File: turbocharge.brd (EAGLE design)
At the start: 56.2 x 21 mm, 87 parts, among them Q1 NMOS40V_10A, Q11 NMOS40V_10A, Q12 NMOS40V_10A, Q14 NMOS40V_10A, Q16 2PMOS50V_0.17A, Q18 NMOS40V_10A, Q2 NMOS40V_10A, Q21 PMOS30V_11A, Q22 PMOS30V_11A, Q23 NMOS40V_10A, Q24 NMOS40V_10A, Q25 PMOS30V_11A, Q26 PMOS30V_11A, Q27 NMOS40V_10A, Q28 NMOS40V_10A, Q31 PMOS30V_11A, Q32 PMOS30V_11A, Q33 PMOS30V_11A, Q34 PMOS30V_11A, Q35 PMOS30V_11A, Q36 PMOS30V_11A, Q37 PMOS30V_11A, Q38 PMOS30V_11A, Q41 PMOS30V_11A, Q42 PMOS30V_11A, Q43 PMOS30V_11A, Q44 PMOS30V_11A, Q45 PMOS30V_11A, Q46 PMOS30V_11A, Q47 PMOS30V_11A, Q48 PMOS30V_11A, Q51 PMOS30V_11A, Q52 PMOS30V_11A, Q53 PMOS30V_11A, Q54 PMOS30V_11A, Q55 PMOS30V_11A, Q56 PMOS30V_11A, Q57 PMOS30V_11A, Q58 PMOS30V_11A, Q62 PMOS30V_11A, Q64 PMOS30V_11A, Q66 PMOS30V_11A, Q68 PMOS30V_11A, T1 TFORM_4_4311_4A4, U1 LT3757IDD, U10 CCR20MA_45V, U2 TC1240A, U4 2NMOS30V_0.1A, U5 74HC595, U6 74HC595

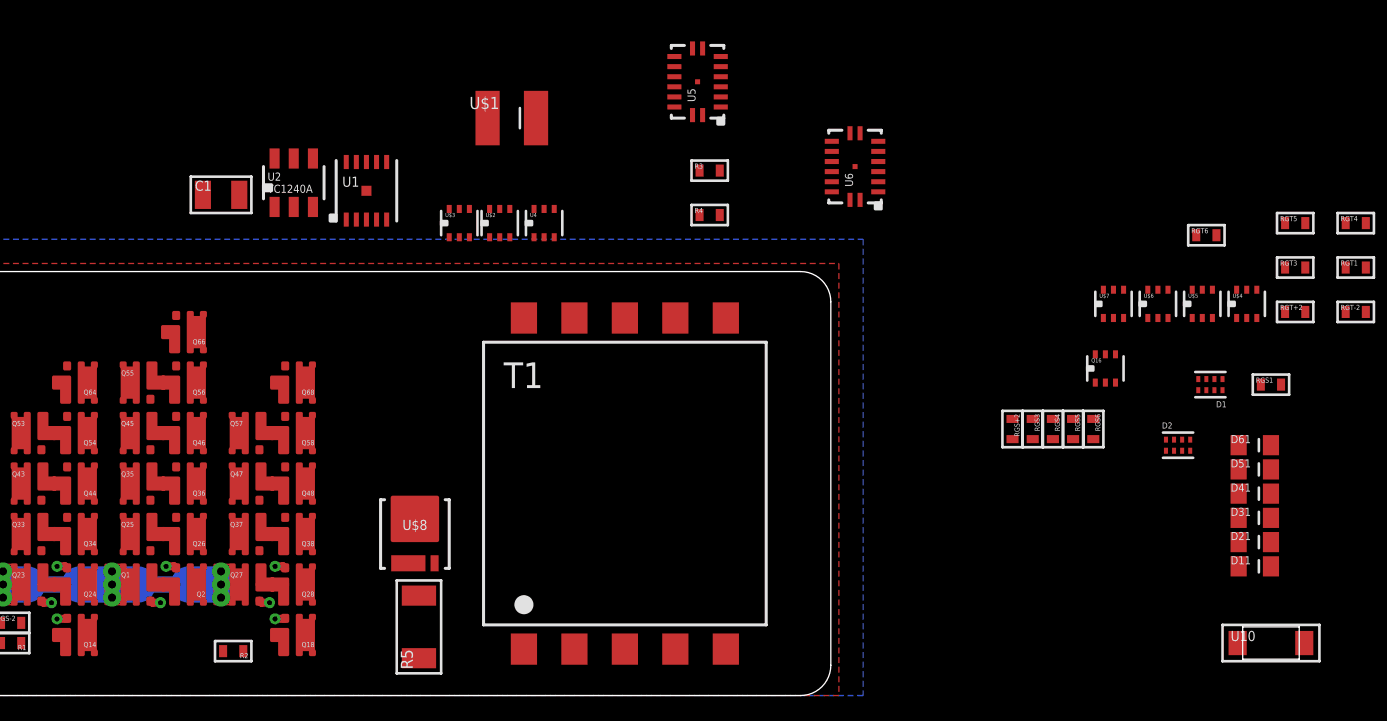
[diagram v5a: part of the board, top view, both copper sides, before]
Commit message: Analog switches are back
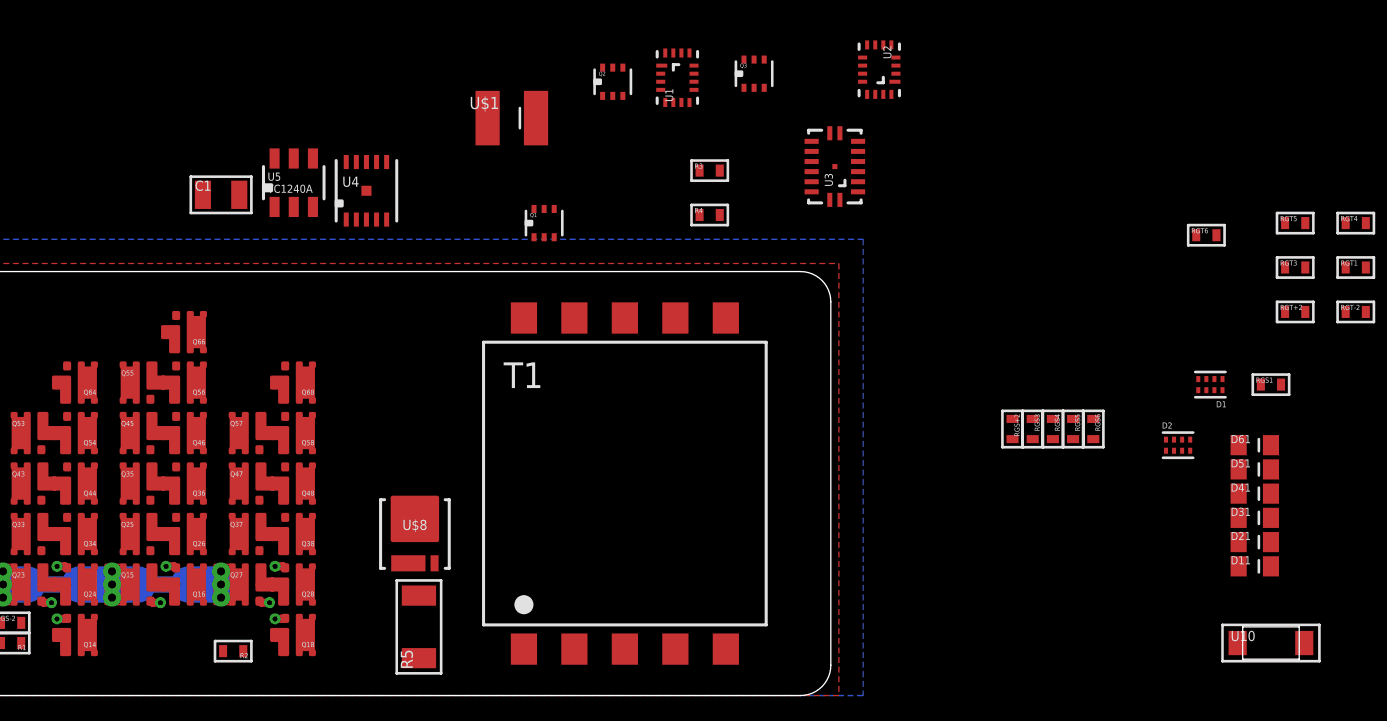
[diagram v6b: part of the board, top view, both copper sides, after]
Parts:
- removed U$2, U$3, U$4, U$5, U$6, U$7: 2NMOS30V_0.1A, dubec:SOT-666
- removed U6: 74HC595, dubec:16-VFQFN
- added Q15: NMOS40V_10A, dubec:6-POWERWDFN
- added Q3: 2PMOS50V_0.17A, dubec:SOT-666
- added U3: 74HC595, dubec:16-VFQFN
- Q1: value NMOS40V_10A -> 2NMOS30V_0.1A; device dubec:6-POWERWDFN -> dubec:SOT-666
- Q16: value 2PMOS50V_0.17A -> NMOS40V_10A; device dubec:SOT-666 -> dubec:6-POWERWDFN
- Q2: value NMOS40V_10A -> 2PMOS50V_0.17A; device dubec:6-POWERWDFN -> dubec:SOT-666
- U1: value LT3757IDD -> DG508BEN-T1-GE4; device dubec:10-WFDFN -> dubec:MINIQFN-16L
- U2: value TC1240A -> DG508BEN-T1-GE4; device dubec:SOT-23-6 -> dubec:MINIQFN-16L
- U4: value 2NMOS30V_0.1A -> LT3757IDD; device dubec:SOT-666 -> dubec:10-WFDFN
- U5: value 74HC595 -> TC1240A; device dubec:16-VFQFN -> dubec:SOT-23-6
- moved Q16 46.6 mm to (24.5, 5.50), turned to 180 degrees
- moved Q2 32.5 mm to (45.4, 30.4), turned to 0 degrees
- moved U2 29.5 mm to (58.6, 31.0), turned to 180 degrees
- moved Q1 27.0 mm to (42.0, 23.4)
- moved U5 20.6 mm to (29.6, 25.4), turned to 0 degrees
- moved U1 16.4 mm to (48.6, 30.6)
- moved U4 8.94 mm to (33.2, 25.0)
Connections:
- removed net !RESET: R4.2, U5.10, U6.10
- removed net DSS: U5.14
- removed net DST: U5.9, U6.14
- removed net EN_S2: U4.2, U5.1
- removed net EN_S3: U$2.2, U5.2
- removed net EN_S4: U$2.5, U5.3
- removed net EN_S5: U$3.2, U5.4
- removed net EN_S6: U$3.5, U5.5
- removed net EN_T1: U$4.2, U6.15
- removed net EN_T2: U$4.5, U$5.2, U6.1
- removed net EN_T3: U$5.5, U6.2
- removed net EN_T4: U$6.2, U6.3
- removed net EN_T5: U$6.5, U6.4
- removed net EN_T6: U$7.2, U6.5
- removed net N$20: U5.7
- removed net N$3: U6.6
- new net AS0: U1.15, U3.1
- new net AS1: U1.14, U3.2
- new net AS2: U1.13, U3.3
- new net AT0: U2.15, U3.4
- new net AT1: U2.14, U3.5
- new net AT2: U2.13, U3.6
- new net DS: U3.14
- new net N$23: Q3.2, U2.3
- net !EN_S1: now also Q1.5, U1.16, U3.15; no longer U4.5, U5.15
- net !OE: now also U3.13; no longer U5.13, U6.13
- net BATT+: now also U1.11, U2.11, U2.16
- net BATT-: now also Q1.4, U1.1, U1.6, U2.1, U2.2, U2.6; no longer R4.1, U$1.C, U$2.1, U$2.4, U$3.1, U$3.4, U$5.1, U$5.4, U$6.1, U$6.4, U$7.1, U4.1, U4.4, U5.8, U5.PAD, U6.8, U6.PAD
- net C1: now also Q15.D; no longer D2.1, D2.2, Q1.D
- net C4+: now also Q2.1, Q3.1, Q3.4; no longer Q16.1, U$4.3, U$4.6
- net CP: now also U3.11, U3.12; no longer U5.11, U5.12, U6.11, U6.12
- net FBX: now also U4.2; no longer U1.2
- net GS+2: now also Q2.2, U1.2; no longer Q16.2, U4.6
- net GS-2: now also Q2.6; no longer Q16.6
- net GS1: now also Q1.3; no longer U4.3
- net GS3: now also U1.3; no longer U$2.6
- net GS4: now also U1.4; no longer U$2.3
- net GS5: now also U1.5; no longer U$3.6
- net GS6: now also U1.10, U1.7, U1.8, U1.9; no longer U$3.3
- net GT+2: now also Q3.5, U2.4; no longer U$5.6
- net GT-2: now also Q3.3; no longer U$4.4
- net GT1: now also Q15.G, Q16.G, Q3.6; no longer Q1.G, Q2.G, U$4.1
- net GT3: now also U2.5; no longer U$5.3
- net GT4: now also U2.10; no longer U$6.6
- net GT5: now also U2.9; no longer U$6.3
- net GT6: now also U2.7, U2.8; no longer U$7.6
- net N$1: now also U3.7; no longer U6.7
- net N$11: now also U4.10, U4.8, U4.9, U5.5; no longer U1.10, U1.8, U1.9, U2.5
- net N$19: now also U3.9; no longer U6.9
- net N$2: now also R4.2, U3.10; no longer U5.6
- net N$5: now also U4.7; no longer U1.7
- net N$7: now also U4.6; no longer U1.6
- net N$8: now also U5.6; no longer U2.6
- net N$9: now also U5.3; no longer U2.3
- net S+: now also D2.1, D2.2, U5.1; no longer U2.1
- net S-: now also R4.1, U$1.C, U1.12, U2.12, U3.8, U3.PAD, U4.5, U4.PAD, U5.2, U5.4; no longer U1.5, U1.PAD, U2.2, U2.4
- net ST+1: now also Q15.S, Q16.S; no longer Q1.S, Q2.S
- net T+: now also Q16.D; no longer Q2.D
- net VCC: now also U3.16; no longer U5.16, U6.16

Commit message: Composing the schematic
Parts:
- added C2: CAP47UF_10V, dubec:0805
- added C3: CAP47NF_16V, dubec:0201P
- added C4: CAP22N_50V, dubec:0402
- added C5: CAP220U_6V3, dubec:1210
- added R6: RES41.2K_16, dubec:0402
- added R7: RES6.8K_16, dubec:0402
- added R8: RES2.2K_16, dubec:0402
- C1: value (none) -> CAP47UF_10V
- moved C1 43.2 mm to (-6.60, -3.60)
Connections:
- removed net N$11: U4.10, U4.8, U4.9, U5.5
- new net N$12: R7.2, U4.1
- new net N$17: C4.2, R7.1
- new net N$3: R6.2, U4.4
- new net N$6: C3.2, U4.3
- new net VCC_REG: C2.2, U4.10, U4.8, U4.9, U5.5
- net BATT-: now also U2.7
- net FBX: now also R8.2
- net GT6: no longer U2.7
- net S+: now also C5.2
- net S-: now also C2.1, C3.1, C4.1, C5.1, R6.1, R8.1
